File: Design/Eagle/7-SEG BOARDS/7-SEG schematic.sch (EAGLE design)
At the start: 2 parts

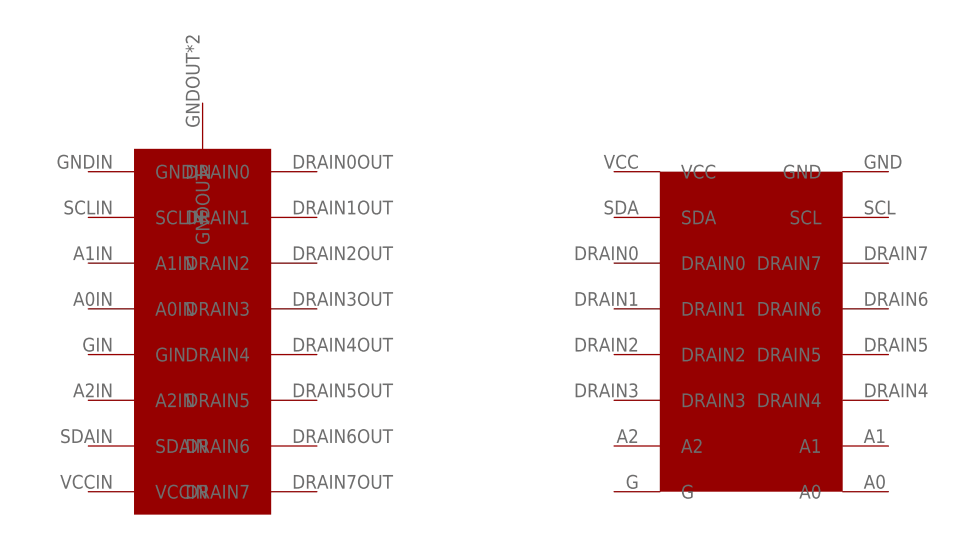
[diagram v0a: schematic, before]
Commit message: Added the 7 segment boards
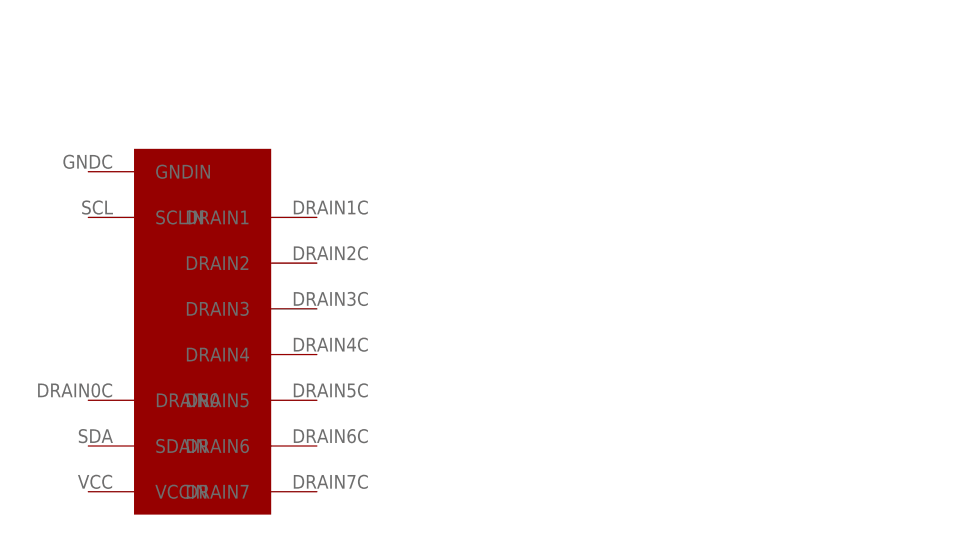
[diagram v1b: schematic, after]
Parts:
- removed U$1: LED_DRIVERBOARD, Parts:LED_DRIVERBOARD
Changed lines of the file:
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@@
 </classes>
 <parts>
-<part name="U$1" library="Parts" deviceset="LED_DRIVERBOARD" device=""/>
 <part name="U$2" library="Parts" deviceset="LED_DRIVER_ASSEMBLY_CHIP" device=""/>
 </parts>
@@
 </plain>
 <instances>
-<instance part="U$1" gate="G$1" x="63.5" y="45.72" rot="R270"/>
 <instance part="U$2" gate="G$1" x="10.16" y="33.02"/>
 </instances>
